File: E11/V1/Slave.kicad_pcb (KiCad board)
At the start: 2 copper layers, 105.2 x 109.2 mm, 420 parts, among them J101 64900221122, J102 64900221122, J1301 64900221122, J1701 64900221122, J201 Header_Male_Pin_2.54mm_1X6_,_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, J202 Header_Male_Pin_2.54mm_1X3_,_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, J2101 64900221122, J2501 64900221122, J300 Header_Male_Pin_2.54mm_1X2_,_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, J401 64900621122, J402 64900621122, J501 64900221122, J901 64900221122, Q101 2N7002P,215, Q1201 CPH6347-TL-W, Q1202 BSS806NH6327XTSA1, Q1301 CPH6347-TL-W, Q1302 CPH6347-TL-W, Q1601 CPH6347-TL-W, Q1602 BSS806NH6327XTSA1, Q1701 CPH6347-TL-W, Q1702 CPH6347-TL-W, Q2001 CPH6347-TL-W, Q2002 BSS806NH6327XTSA1, Q2101 CPH6347-TL-W, Q2102 CPH6347-TL-W, Q2401 CPH6347-TL-W, Q2402 BSS806NH6327XTSA1, Q2501 CPH6347-TL-W, Q2502 CPH6347-TL-W, Q2801 CPH6347-TL-W, Q2802 BSS806NH6327XTSA1, Q501 CPH6347-TL-W, Q502 CPH6347-TL-W, Q801 CPH6347-TL-W, Q802 BSS806NH6327XTSA1, Q901 CPH6347-TL-W, Q902 CPH6347-TL-W, SW101 DIP_SW_3, SW201 PTS645SM43SMTR92, SW202 PTS645SM43SMTR92, U1001 AP3015KTR-G1, U1002 AP2202K-ADJTRG1, U1101 ADC121S021CIMF/NOPB, U1201 ADCMP350YKSZ-REEL7, U1301 LTV-816S, U1302 SI8641AB-B-IS1, U1401 AP3015KTR-G1, U1402 AP2202K-ADJTRG1, U1501 ADC121S021CIMF/NOPB, U1601 ADCMP350YKSZ-REEL7, U1701 LTV-816S, U1702 SI8641AB-B-IS1, U1801 AP3015KTR-G1, U1802 AP2202K-ADJTRG1, U1901 ADC121S021CIMF/NOPB, U2001 ADCMP350YKSZ-REEL7, U201 STM32F446RE, U2101 LTV-816S, U2102 SI8641AB-B-IS1, U2201 AP3015KTR-G1, U2202 AP2202K-ADJTRG1, U2301 ADC121S021CIMF/NOPB, U2401 ADCMP350YKSZ-REEL7, U2501 LTV-816S, U2502 SI8641AB-B-IS1, U2601 AP3015KTR-G1, U2602 AP2202K-ADJTRG1, U2701 ADC121S021CIMF/NOPB, U2801 ADCMP350YKSZ-REEL7, U301 OKI-78SR-5/1.5-W36-C, U302 AZ1117IH-3.3TRG1, U401 SN65HVD232DR, U501 LTV-816S, U502 SI8641AB-B-IS1, U601 AP3015KTR-G1, U602 AP2202K-ADJTRG1, U701 ADC121S021CIMF/NOPB, U801 ADCMP350YKSZ-REEL7, U901 LTV-816S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

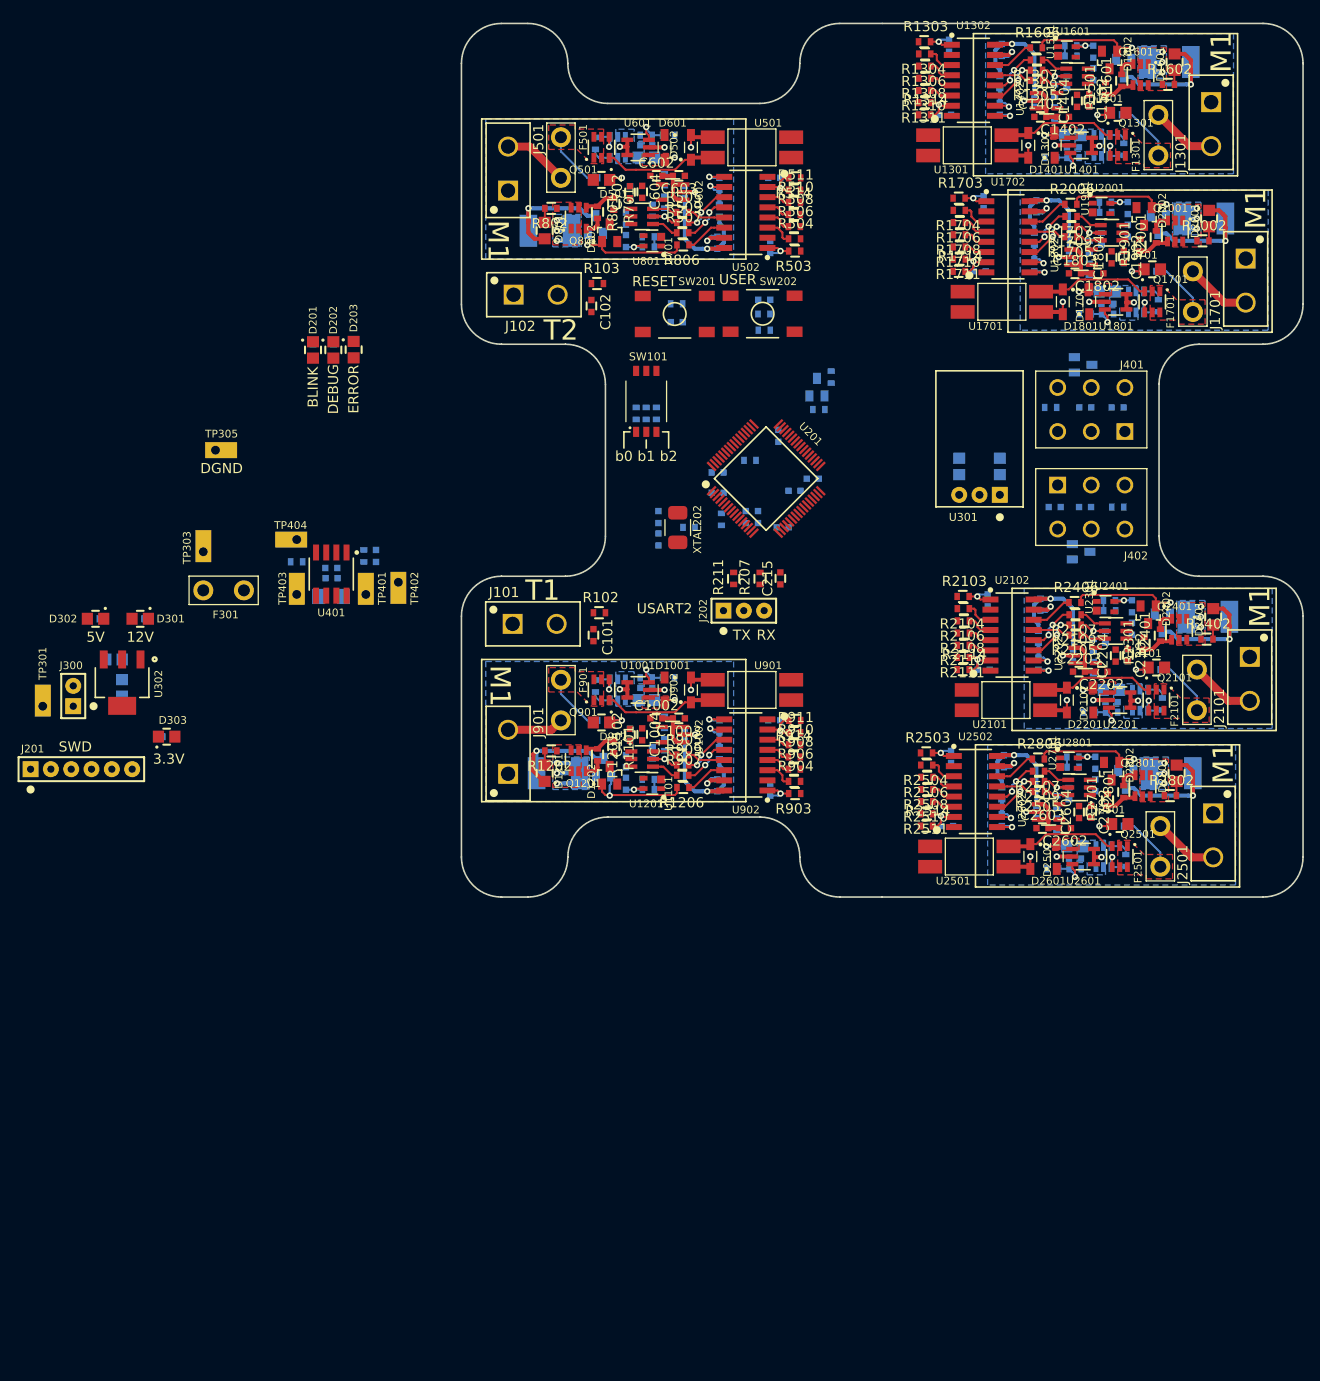
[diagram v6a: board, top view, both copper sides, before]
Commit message: initial component placement done
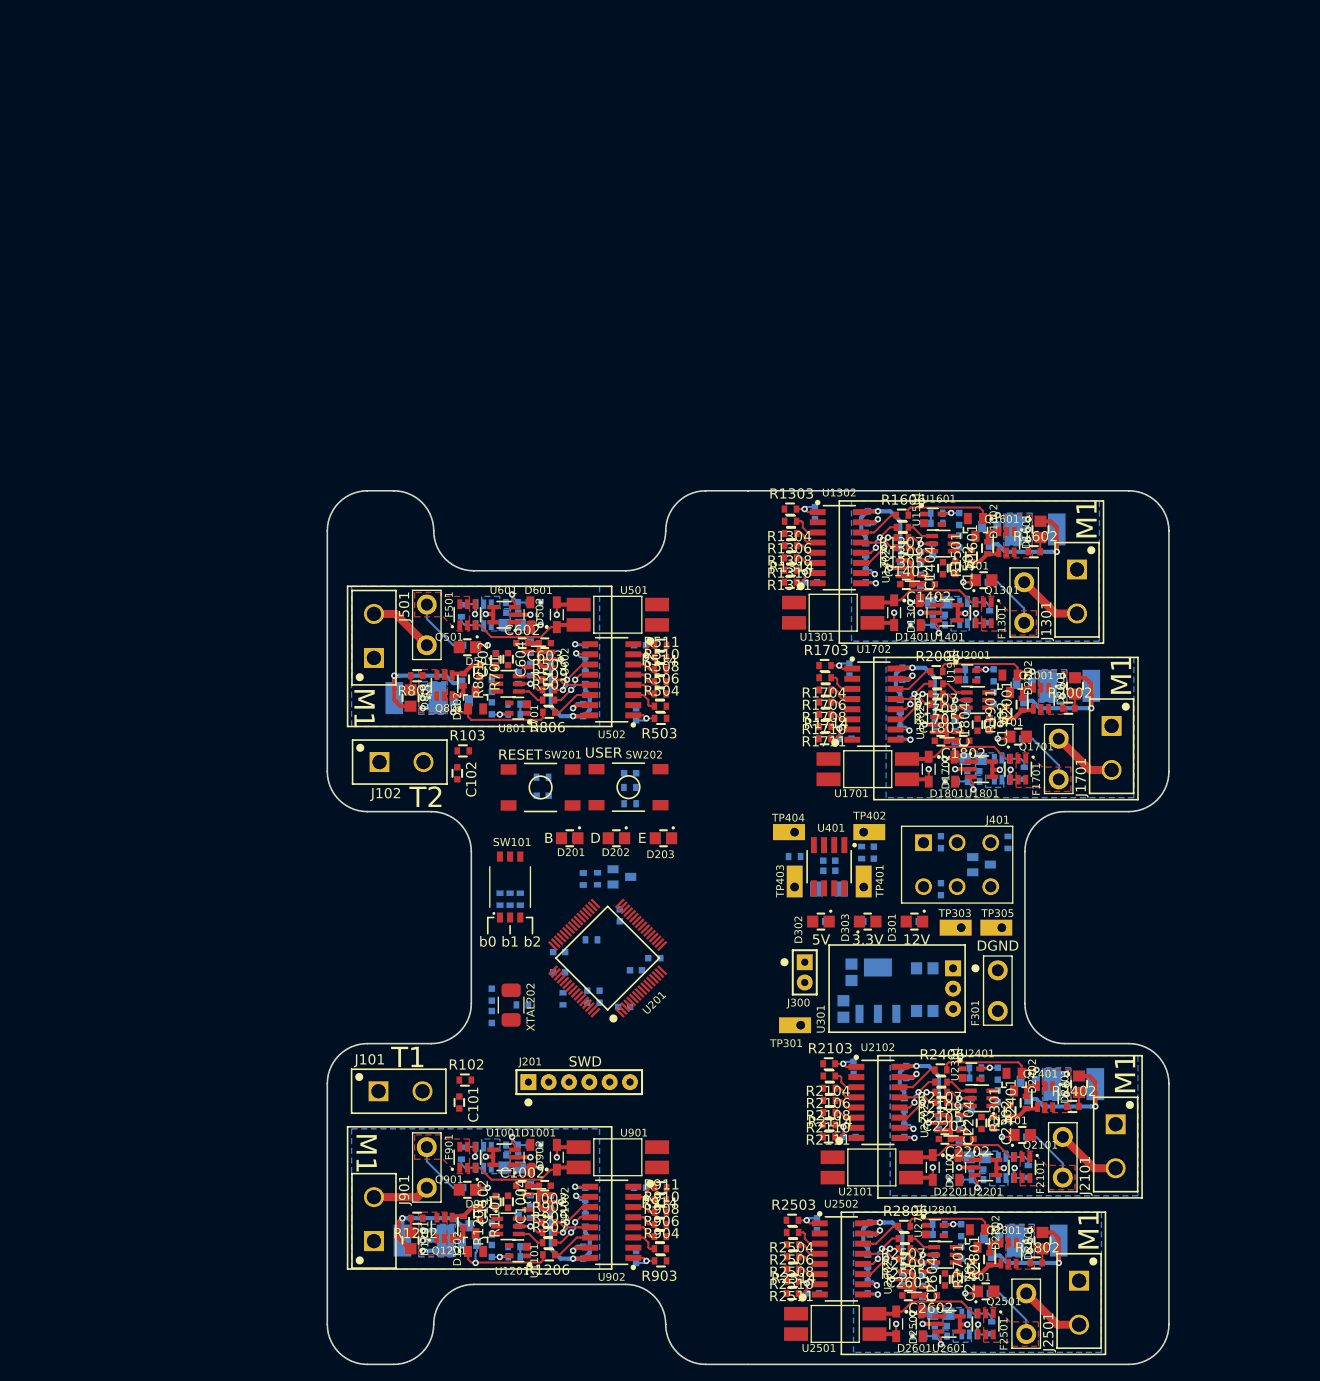
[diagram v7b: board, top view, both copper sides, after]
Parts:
- removed C215, C406, C407: 885012007053, Capacitors:C0603
- removed D402: D1213A-02SOL-7, IC:SOT-23-3
- removed J202: Header_Male_Pin_2.54mm_1X3_,_Unshrouded, Connectors:Headers_2.54mm_1X3
- removed J402: 64900621122, Connectors:64900621122
- removed R207: RC0805JR-074K7L, Resistors:R0603
- removed R211: RC0805JR-071KL, Resistors:R0603
- removed R404: RC0805JR-070RL, Resistors:R0603
- U302: moved to B.Cu
- moved TP305 115.0 mm to (238.0, 137.9), turned to 180 degrees
- moved F301 108.9 mm to (237.5, 145.8), turned to 270 degrees
- moved TP303 105.8 mm to (232.9, 137.9), turned to 180 degrees
- moved D301 103.9 mm to (228.1, 137.2)
- moved R301 103.9 mm to (226.0, 137.2)
- moved TP301 102.8 mm to (212.9, 150.1), turned to 180 degrees
- moved U302 102.0 mm to (222.5, 145.8)
- moved C304 99.7 mm to (218.2, 147.1), turned to 270 degrees
- moved C301 98.6 mm to (219.2, 144.5), turned to 90 degrees
- moved R302 98.3 mm to (214.4, 137.2)
- moved D302 98.3 mm to (216.4, 137.2)
- moved J300 96.9 mm to (213.4, 142.2), turned to 270 degrees
- moved D303 90.6 mm to (220.2, 137.2)
- moved R303 90.6 mm to (222.2, 137.2)
- moved D203 73.7 mm to (196.7, 126.7), turned to 180 degrees
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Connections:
- U201 pad 16: /STM32F446/PA2 -> (no net)
- U201 pad 17: /STM32F446/PA3 -> (no net)
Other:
- board text added: "B"
- board text added: "D"
- board text added: "E"
- board text removed: "BLINK"
- board text removed: "DEBUG"
- board text removed: "ERROR"
- board text removed: "RX"
- board text removed: "TX"
- board text removed: "USART2"

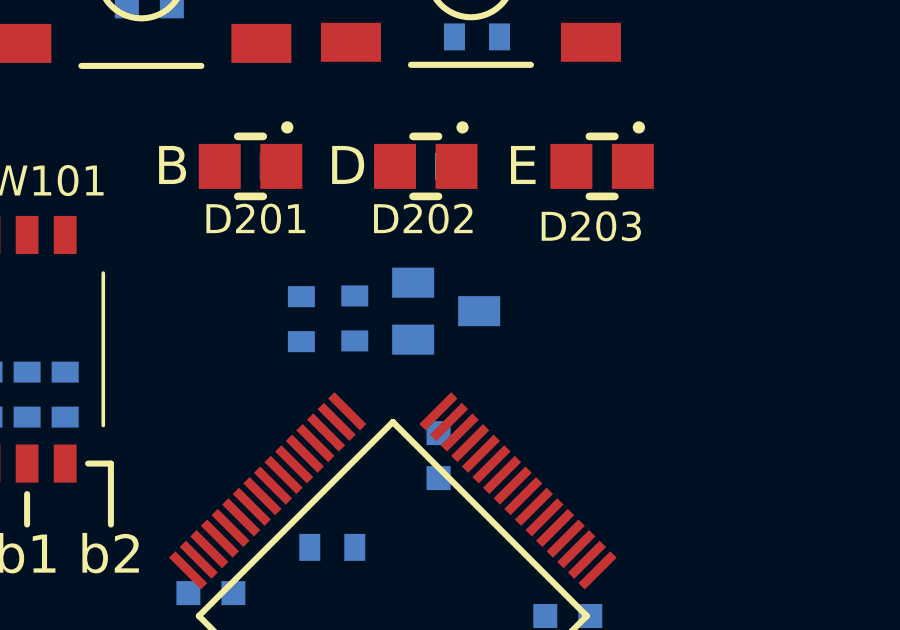
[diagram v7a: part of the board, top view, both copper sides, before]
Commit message: updated filter values and pcb
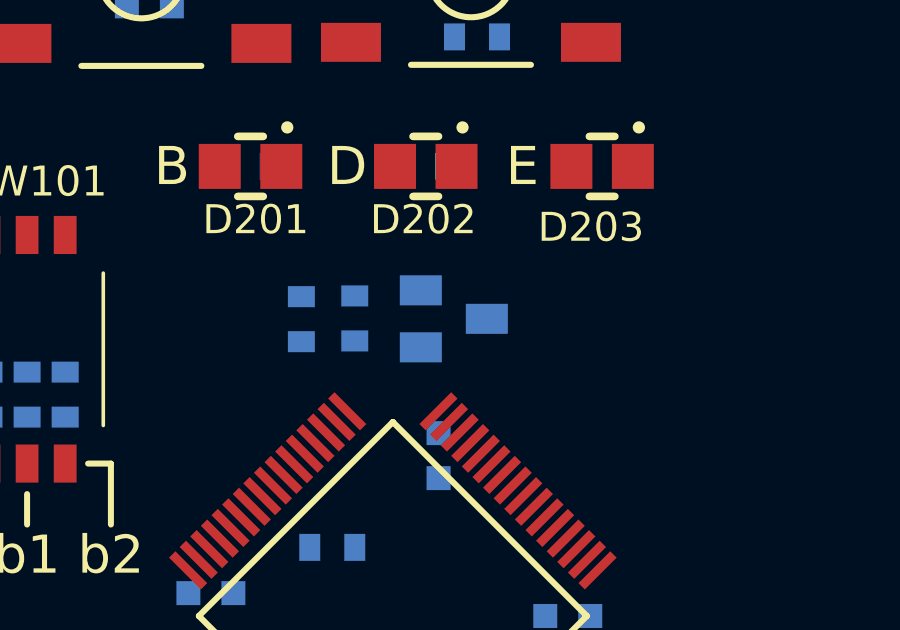
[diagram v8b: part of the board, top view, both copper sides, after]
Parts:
- moved Q101 0.36 mm to (190.8, 131.8)
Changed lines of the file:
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@@
   )
   (module IC:SOT-23-3 (layer B.Cu)
-    (at 190.5 131.572 90)
+    (at 190.754 131.826 90)
     (fp_text reference Q101 (at 0.03 2.97 270) (layer B.SilkS)
       (effects (font (size 0.9652 0.9652) (thickness 0.2032)) (justify mirror))
